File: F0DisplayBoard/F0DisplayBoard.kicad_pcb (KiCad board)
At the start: 2 copper layers, 8 parts, among them J1 NHD-C0216CZ-FSW-FBW-3V3, U1 STM32F051R8T6TR, U2 ROTARY_ENC_PEC12R, U3 AZ1117EH-3.3TRG1, U4 FT232RLREEL, X1 ABLS7M2_16MHz_XTAL

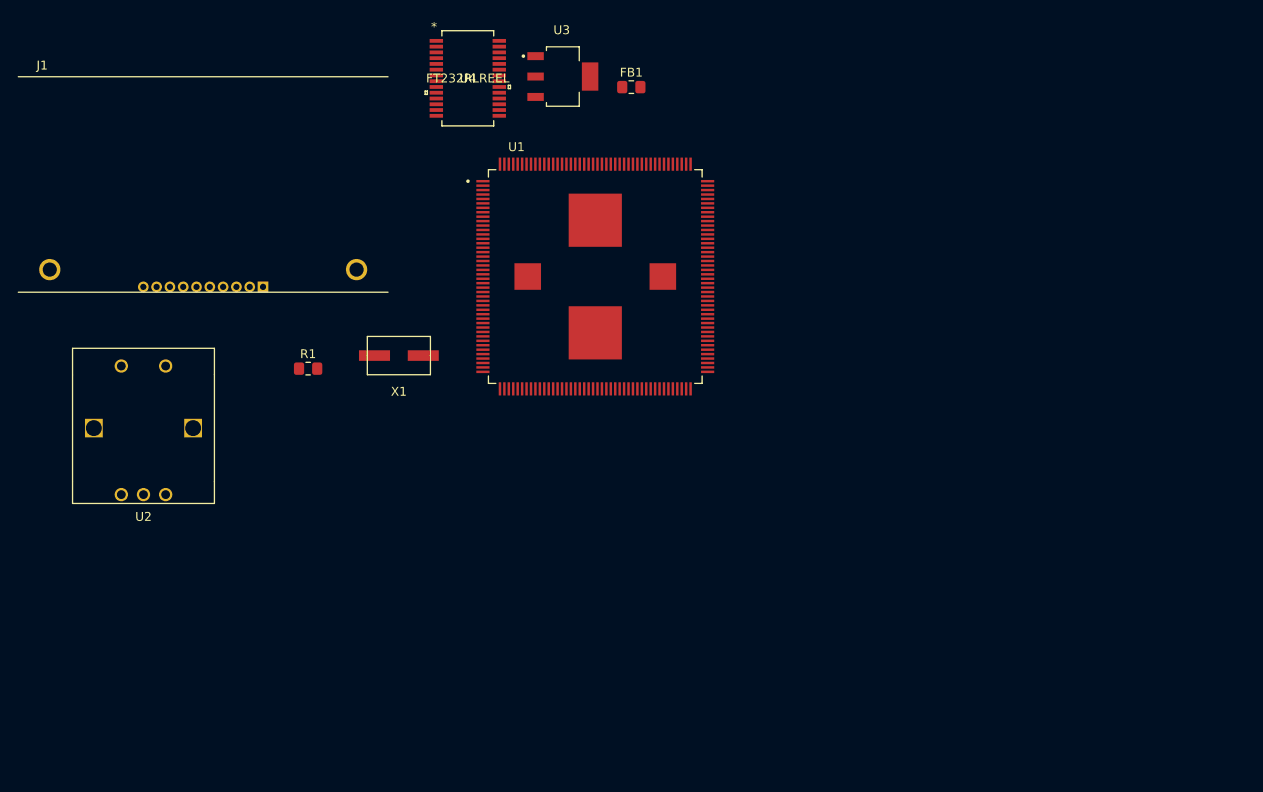
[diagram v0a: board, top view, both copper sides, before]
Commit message: sch: Removed some connectors to make room on board. pcb: rough routing, difficulty with traces cutting into planes. May restart routing of most signals
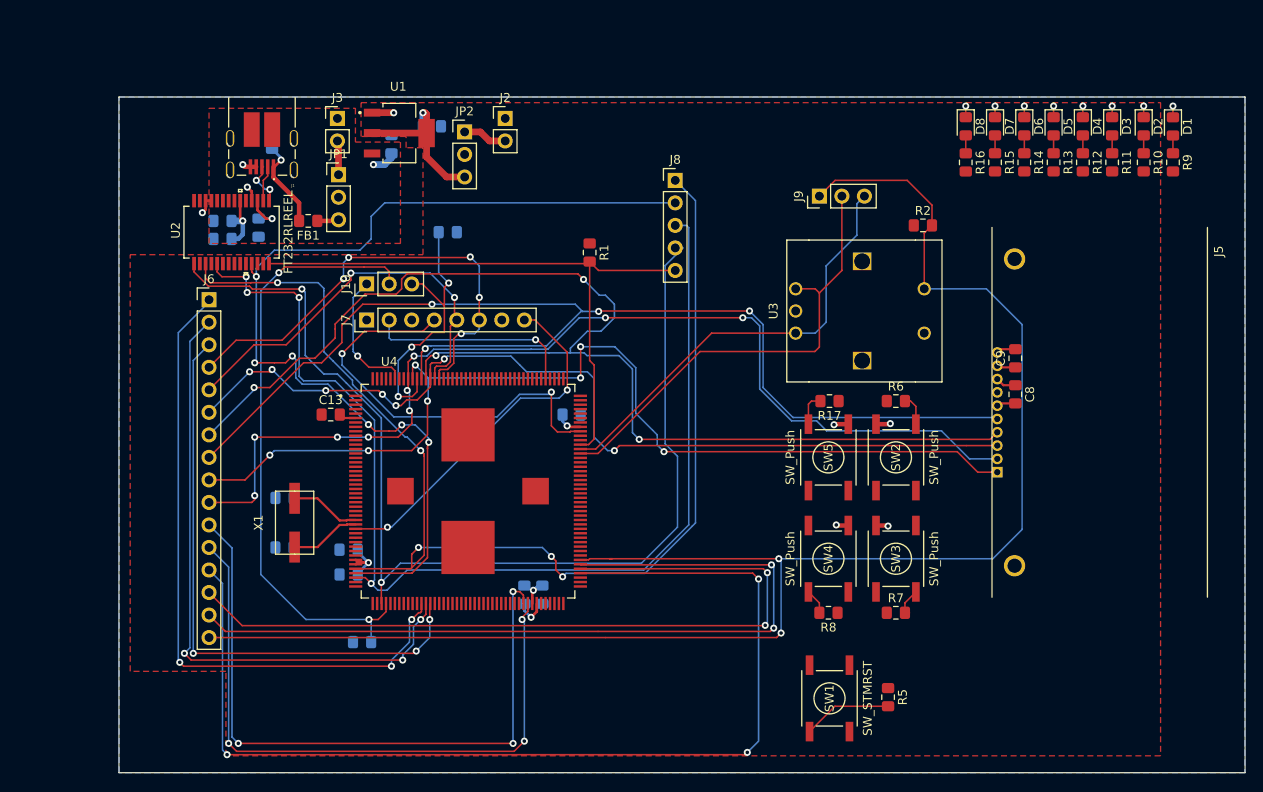
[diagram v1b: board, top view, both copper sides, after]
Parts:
- added C1: 1uF, Capacitor_SMD:C_0805_2012Metric_Pad1.15x1.40mm_HandSolder, B.Cu at (123.4, 70.1)
- added C10: 31pF, Capacitor_SMD:C_0805_2012Metric_Pad1.15x1.40mm_HandSolder, B.Cu at (111.4, 115.6)
- added C11: 100nF, Capacitor_SMD:C_0805_2012Metric_Pad1.15x1.40mm_HandSolder, B.Cu at (140.5, 120.9)
- added C12: 100nF, Capacitor_SMD:C_0805_2012Metric_Pad1.15x1.40mm_HandSolder, B.Cu at (143.8, 100.6)
- added C13: 100nF, Capacitor_SMD:C_0805_2012Metric_Pad1.15x1.40mm_HandSolder, F.Cu at (116.6, 100.6)
- added C14: 4.7uF, Capacitor_SMD:C_0805_2012Metric_Pad1.15x1.40mm_HandSolder, B.Cu at (138.4, 120.9)
- added C15: 10nF, Capacitor_SMD:C_0805_2012Metric_Pad1.15x1.40mm_HandSolder, B.Cu at (118.6, 118.6)
- added C16: 1uF, Capacitor_SMD:C_0805_2012Metric_Pad1.15x1.40mm_HandSolder, B.Cu at (118.6, 115.8)
- added C2: 100nF, Capacitor_SMD:C_0805_2012Metric_Pad1.15x1.40mm_HandSolder, B.Cu at (104.4, 80.8)
- added C3: 10nF, Capacitor_SMD:C_0805_2012Metric_Pad1.15x1.40mm_HandSolder, B.Cu at (110.0, 69.6)
- added C4: 4.7uF, Capacitor_SMD:C_0805_2012Metric_Pad1.15x1.40mm_HandSolder, B.Cu at (104.4, 78.7)
- added C5: 100nF, Capacitor_SMD:C_0805_2012Metric_Pad1.15x1.40mm_HandSolder, B.Cu at (108.5, 79.5)
- added C6: 1uF, Capacitor_SMD:C_0805_2012Metric_Pad1.15x1.40mm_HandSolder, B.Cu at (128.0, 68.1)
- added C7: 31pf, Capacitor_SMD:C_0805_2012Metric_Pad1.15x1.40mm_HandSolder, B.Cu at (111.4, 110.0)
- added C8: 1uF, Capacitor_SMD:C_0805_2012Metric_Pad1.15x1.40mm_HandSolder, F.Cu at (193.8, 98.3)
- added C9: 1uF, Capacitor_SMD:C_0805_2012Metric_Pad1.15x1.40mm_HandSolder, F.Cu at (193.8, 94.2)
- added D1: LED, LED_SMD:LED_0805_2012Metric_Pad1.15x1.40mm_HandSolder, F.Cu at (211.6, 68.1)
- added D2: LED, LED_SMD:LED_0805_2012Metric_Pad1.15x1.40mm_HandSolder, F.Cu at (208.3, 68.1)
- added D3: LED, LED_SMD:LED_0805_2012Metric_Pad1.15x1.40mm_HandSolder, F.Cu at (204.7, 68.1)
- added D4: LED, LED_SMD:LED_0805_2012Metric_Pad1.15x1.40mm_HandSolder, F.Cu at (201.4, 68.1)
- added D5: LED, LED_SMD:LED_0805_2012Metric_Pad1.15x1.40mm_HandSolder, F.Cu at (198.1, 68.1)
- added D6: LED, LED_SMD:LED_0805_2012Metric_Pad1.15x1.40mm_HandSolder, F.Cu at (194.8, 68.1)
- added D7: LED, LED_SMD:LED_0805_2012Metric_Pad1.15x1.40mm_HandSolder, F.Cu at (191.5, 68.1)
- added D8: LED, LED_SMD:LED_0805_2012Metric_Pad1.15x1.40mm_HandSolder, F.Cu at (188.2, 68.1)
- added J1: USB_B_Micro, MICROUSB:CUIDEVICES_UJ2-MIBH-4-SMT-TR, F.Cu at (108.8, 67.7)
- added J10: CONN_STMPWR, Connector_PinHeader_2.54mm:PinHeader_1x03_P2.54mm_Vertical, F.Cu at (120.7, 85.9)
- added J2: CONN_3V3, Connector_PinHeader_2.54mm:PinHeader_1x02_P2.54mm_Vertical, F.Cu at (136.3, 67.2)
- added J3: CONN_5v, Connector_PinHeader_2.54mm:PinHeader_1x02_P2.54mm_Vertical, F.Cu at (117.3, 67.2)
- added J6: CONN_PB, Connector_PinHeader_2.54mm:PinHeader_1x16_P2.54mm_Vertical, F.Cu at (102.9, 87.6)
- added J7: CONN_DEBUG, Connector_PinHeader_2.54mm:PinHeader_1x08_P2.54mm_Vertical, F.Cu at (120.7, 89.9)
- added J8: CONN_FTDI, Connector_PinHeader_2.54mm:PinHeader_1x05_P2.54mm_Vertical, F.Cu at (155.4, 74.2)
- added J9: CONN_ROT, Connector_PinHeader_2.54mm:PinHeader_1x03_P2.54mm_Vertical, F.Cu at (171.7, 75.9)
- added JP1: Jumper_3_Open, Connector_PinHeader_2.54mm:PinHeader_1x03_P2.54mm_Vertical, F.Cu at (117.5, 73.5)
- added JP2: Jumper_3_Open, Connector_PinHeader_2.54mm:PinHeader_1x03_P2.54mm_Vertical, F.Cu at (131.7, 68.7)
- added R1: 1K, Resistor_SMD:R_0805_2012Metric_Pad1.15x1.40mm_HandSolder, F.Cu at (145.8, 82.3)
- added R10: 1K, Resistor_SMD:R_0805_2012Metric_Pad1.15x1.40mm_HandSolder, F.Cu at (208.3, 72.1)
- added R11: 1K, Resistor_SMD:R_0805_2012Metric_Pad1.15x1.40mm_HandSolder, F.Cu at (204.7, 72.1)
- added R12: 1K, Resistor_SMD:R_0805_2012Metric_Pad1.15x1.40mm_HandSolder, F.Cu at (201.4, 72.1)
- added R13: 1K, Resistor_SMD:R_0805_2012Metric_Pad1.15x1.40mm_HandSolder, F.Cu at (198.1, 72.1)
- added R14: 1K, Resistor_SMD:R_0805_2012Metric_Pad1.15x1.40mm_HandSolder, F.Cu at (194.8, 72.1)
- added R15: 1K, Resistor_SMD:R_0805_2012Metric_Pad1.15x1.40mm_HandSolder, F.Cu at (191.5, 72.1)
- added R16: 1K, Resistor_SMD:R_0805_2012Metric_Pad1.15x1.40mm_HandSolder, F.Cu at (188.2, 72.1)
- added R17: 1K, Resistor_SMD:R_0805_2012Metric_Pad1.15x1.40mm_HandSolder, F.Cu at (172.8, 99.1)
- added R3: 10K, Resistor_SMD:R_0805_2012Metric_Pad1.15x1.40mm_HandSolder, B.Cu at (120.1, 126.2)
- added R4: 10K, Resistor_SMD:R_0805_2012Metric_Pad1.15x1.40mm_HandSolder, B.Cu at (129.8, 80.0)
- added R5: 1K, Resistor_SMD:R_0805_2012Metric_Pad1.15x1.40mm_HandSolder, F.Cu at (179.5, 132.5)
- added R6: 1K, Resistor_SMD:R_0805_2012Metric_Pad1.15x1.40mm_HandSolder, F.Cu at (180.3, 99.1)
- added R7: 1K, Resistor_SMD:R_0805_2012Metric_Pad1.15x1.40mm_HandSolder, F.Cu at (180.3, 122.9)
- added R8: 1K, Resistor_SMD:R_0805_2012Metric_Pad1.15x1.40mm_HandSolder, F.Cu at (172.7, 122.9)
- added R9: 1K, Resistor_SMD:R_0805_2012Metric_Pad1.15x1.40mm_HandSolder, F.Cu at (211.6, 72.1)
- added SW1: SW_STMRST, TACTILE_SW:PTS645SK43SMTR92LFS, F.Cu at (172.8, 132.6)
- added SW2: SW_Push, TACTILE_SW:PTS645SK43SMTR92LFS, F.Cu at (180.3, 105.4)
- added SW3: SW_Push, TACTILE_SW:PTS645SK43SMTR92LFS, F.Cu at (180.3, 116.8)
- added SW4: SW_Push, TACTILE_SW:PTS645SK43SMTR92LFS, F.Cu at (172.7, 116.8)
- added SW5: SW_Push, TACTILE_SW:PTS645SK43SMTR92LFS, F.Cu at (172.7, 105.4)
- U1: value STM32F051R8T6TR -> AZ1117EH-3.3TRG1; footprint STM32F051R8T6:QFP50P2600X2600X160-176N -> 3V3_Regulator:SOT230P700X180-4N
- U2: value ROTARY_ENC_PEC12R -> FT232RLREEL; footprint ROTARY_ENC_PEC12R:ROTARY_ENC_PEC12R -> ft232r:FT232RLREEL
- U3: value AZ1117EH-3.3TRG1 -> ROTARY_ENC_PEC12R; footprint 3V3_Regulator:SOT230P700X180-4N -> ROTARY_ENC_PEC12R:ROTARY_ENC_PEC12R
- U4: value FT232RLREEL -> STM32F051R8T6TR; footprint ft232r:FT232RLREEL -> STM32F051R8T6:QFP50P2600X2600X160-176N
- moved J5 90.7 mm to (191.8, 100.3), turned to 270 degrees
- moved R2 71.2 mm to (183.4, 79.2)
- moved U4 46.6 mm to (132.1, 109.2)
- moved U3 42.9 mm to (176.5, 88.9), turned to 270 degrees
- moved FB1 39.4 mm to (114.1, 78.7), turned to 180 degrees
- moved U1 27.4 mm to (124.3, 68.8)
- moved U2 24.2 mm to (105.4, 80.0), turned to 90 degrees
- moved X1 22.2 mm to (112.5, 112.8), turned to 270 degrees
- renumbered J1 to J5, R1 to R2
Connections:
- net Net-(U4-Pad10) renamed /PC15
- net Net-(U4-Pad8) renamed /PC13
- net Net-(U4-Pad9) renamed /PC14
- FB1 pad 1: +5V -> /VUSB
- FB1 pad 2: Net-(C5-Pad1) -> /VBUS
- U1 pad 1: Net-(U1-Pad1) -> GND
- U1 pad 2: Net-(U1-Pad2) -> /3.3V_AZ
- U1 pad 3: Net-(U1-Pad3) -> +5V
- U1 pad 4: Net-(U1-Pad4) -> /3.3V_AZ
- U2 pad 1: /ROT_SW1 -> /FT_TX
- U2 pad 2: GND -> Net-(U2-Pad2)
- U2 pad 3: /ROT_CHA -> /FT_RTS
- U2 pad 4: GND -> +3V3
- U2 pad 5: /ROT_CHB -> /FT_RX
- U3 pad 1: GND -> /ROT_SW1
- U3 pad 2: +3V3 -> GND
- U3 pad 3: +5V -> /ROT_CHA
- U3 pad 4: +3V3 -> GND
- U4 pad 1: /FT_TX -> Net-(U4-Pad1)
- U4 pad 11: /FT_CTS -> Net-(U4-Pad11)
- U4 pad 14: /FT_PWREN -> GND
- U4 pad 15: Net-(J2-Pad3) -> +3V3
- U4 pad 18: GND -> Net-(U4-Pad18)
- U4 pad 20: +5V -> Net-(U4-Pad20)
- U4 pad 21: GND -> Net-(U4-Pad21)
- U4 pad 22: Net-(U4-Pad22) -> GND
- U4 pad 23: Net-(U4-Pad23) -> +3V3
- U4 pad 25: GND -> Net-(U4-Pad25)
- U4 pad 26: GND -> Net-(U4-Pad26)
- U4 pad 3: /FT_RTS -> Net-(U4-Pad3)
- U4 pad 4: +3V3 -> Net-(U4-Pad4)
- U4 pad 5: /FT_RX -> Net-(U4-Pad5)
- U4 pad 6: Net-(U4-Pad6) -> /VBAT
- U4 pad 7: GND -> Net-(U4-Pad7)
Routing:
- net /ROT_SW1: track 0.00 -> 184.9 mm, vias 0 -> 2
- net /DISP_SCL: track 0.00 -> 140.2 mm, vias 0 -> 4
- net /FT_RTS: track 0.00 -> 136.9 mm, vias 0 -> 5
- net /DISP_SI: track 0.00 -> 129.9 mm, vias 0 -> 4
- net /FT_RX: track 0.00 -> 126.7 mm, vias 0 -> 4
- net /FT_TX: track 0.00 -> 124.1 mm, vias 0 -> 2
- net /PB12: track 0.00 -> 120.9 mm, vias 0 -> 3
- net /DISP_RS: track 0.00 -> 117.2 mm, vias 0 -> 9
- net /DISP_RST: track 0.00 -> 114.2 mm, vias 0 -> 7
- net /FT_CTS: track 0.00 -> 112.2 mm, vias 0 -> 6
- net /DISP_CSB: track 0.00 -> 106.3 mm, vias 0 -> 7
- net /PB14: track 0.00 -> 93.4 mm, vias 0 -> 2
- net /PB13: track 0.00 -> 91.6 mm, vias 0 -> 2
- net /PB10: track 0.00 -> 76.4 mm, vias 0 -> 3
- net /PB0: track 0.00 -> 75.0 mm, vias 0 -> 3
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- added copper zone on F.Cu, net +3V3
- added copper zone on F.Cu, net +5V
- added copper zone on B.Cu, net GND
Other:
- board outline added: 127 x 76.2 mm
- rule trace_min: 0.2 -> 0.1778

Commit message: pcb: re-routed mostlyl orthogonally. Still need to get 3.3V plane to reach some pins and check other "unrouted" signals
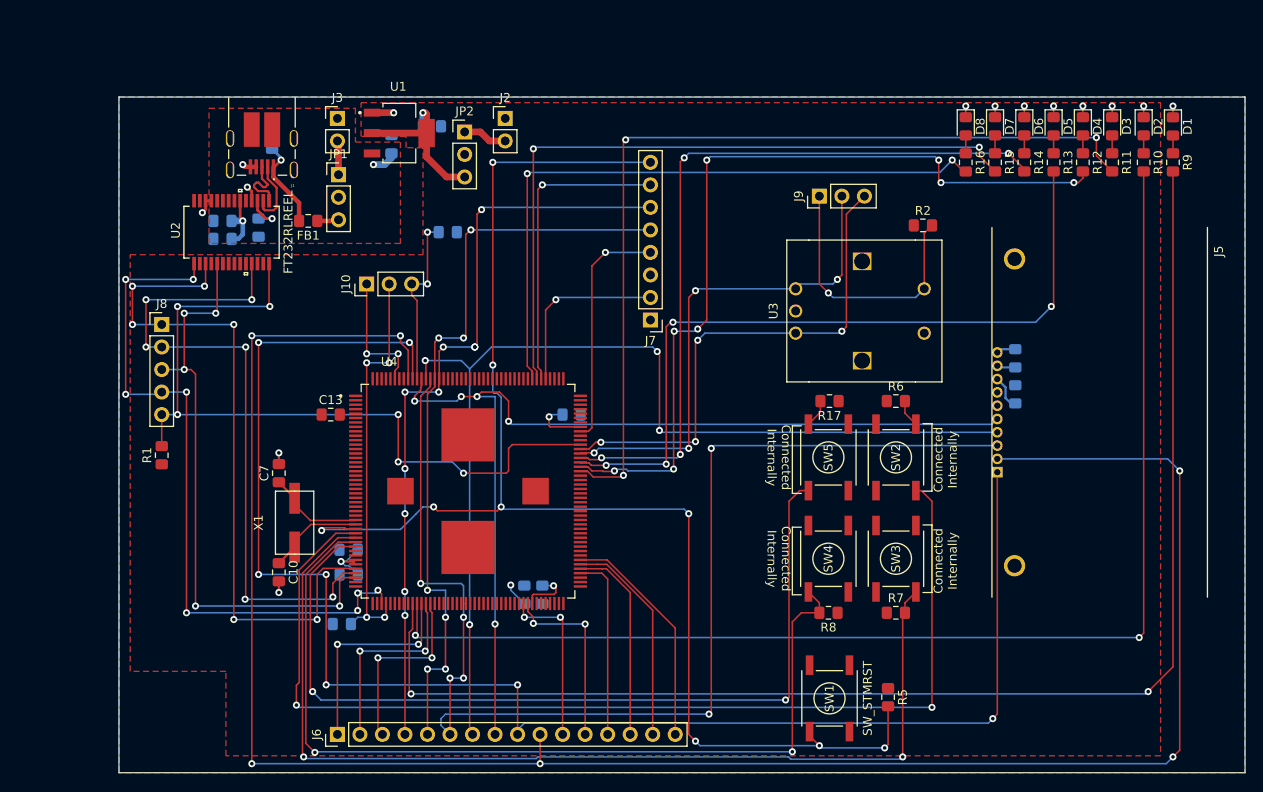
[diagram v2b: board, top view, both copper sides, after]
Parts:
- C10, C7: moved to F.Cu
- C8, C9: moved to B.Cu
- moved J8 60.2 mm to (97.5, 90.4)
- moved R1 53.4 mm to (97.5, 105.2), turned to 90 degrees
- moved J6 51.1 mm to (117.3, 136.7), turned to 90 degrees
- moved J7 32.0 mm to (152.7, 89.9), turned to 180 degrees
- moved R3 3.06 mm to (117.8, 124.2)
- moved C7 2.87 mm to (110.7, 107.2), turned to 90 degrees
- moved C10 2.87 mm to (110.7, 118.4), turned to 270 degrees
- turned C8 to 90 degrees
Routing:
- net /PC4: track 0.00 -> 153.5 mm, vias 0 -> 2
- net /PC5: track 0.00 -> 138.2 mm, vias 0 -> 2
- net /ROT_SW1: track 184.9 -> 56.2 mm, vias 2 -> 1
- net /PC0: track 3.49 -> 123.9 mm, vias 0 -> 2
- net /DISP_RS: track 117.2 -> 231.5 mm, vias 9 -> 6
- net /PC1: track 3.45 -> 115.6 mm, vias 0 -> 2
- net /NRST: track 51.0 -> 159.0 mm, vias 2 -> 9
- net /PC6: track 0.00 -> 100.9 mm, vias 0 -> 3
- net /PB12: track 120.9 -> 20.9 mm, vias 3 -> 0
- net /PC2: track 2.86 -> 102.5 mm, vias 0 -> 2
- net /PC3: track 3.75 -> 101.9 mm, vias 0 -> 2
- net /PC7: track 0.06 -> 95.2 mm, vias 0 -> 8
- net /PC8: track 0.00 -> 85.1 mm, vias 0 -> 4
- net /PC9: track 0.00 -> 84.8 mm, vias 0 -> 4
- net /PC10: track 0.00 -> 79.9 mm, vias 0 -> 2
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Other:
- board text added: "Connected Internally"

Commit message: Rev2 completed   -Added current-limiting resitstor for LCD backlight   -Fixed microcontroller footprint   -Board size reduced
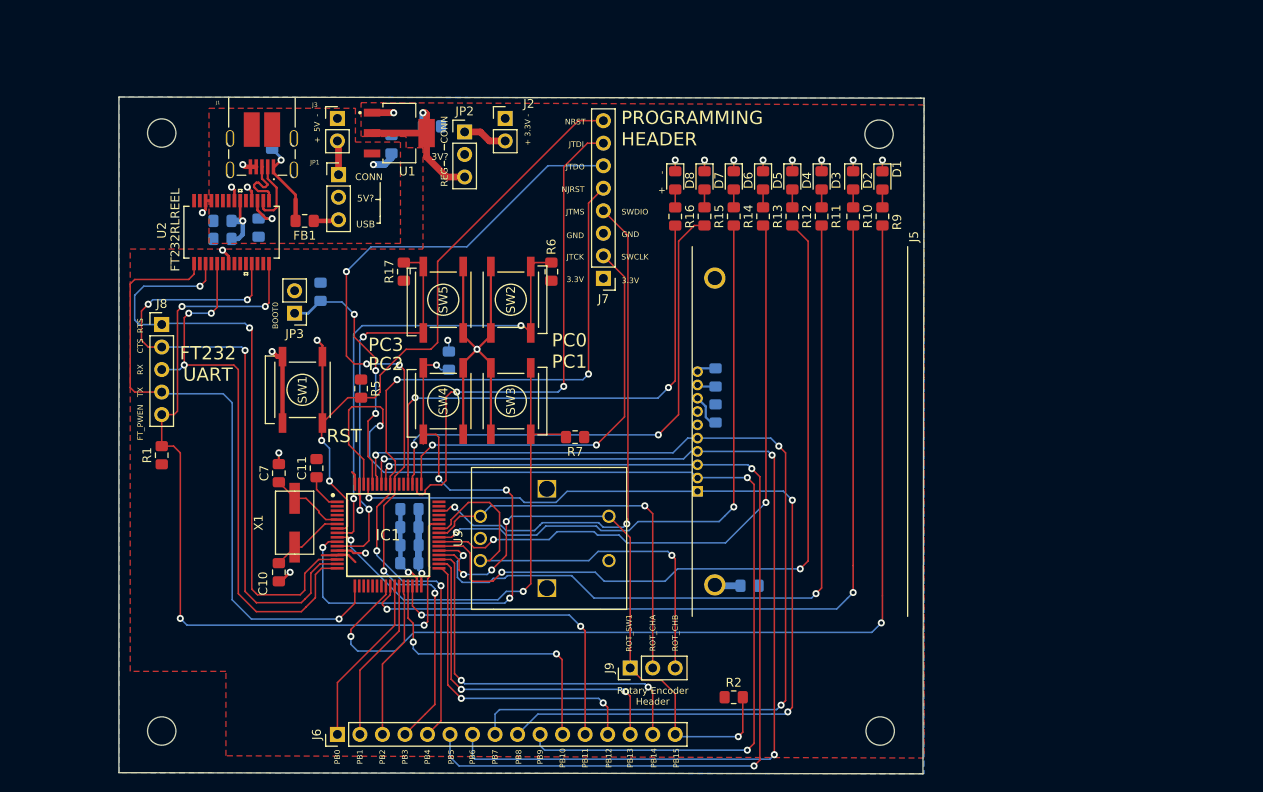
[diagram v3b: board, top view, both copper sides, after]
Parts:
- removed C16: 1uF, Capacitor_SMD:C_0805_2012Metric_Pad1.15x1.40mm_HandSolder
- removed J10: CONN_STMPWR, Connector_PinHeader_2.54mm:PinHeader_1x03_P2.54mm_Vertical
- removed U4: STM32F051R8T6TR, STM32F051R8T6:QFP50P2600X2600X160-176N
- added G***: LOGO, Sophie:sophie, B.Cu at (103.3, 118.1)
- added IC1: STM32F051R8T6TR, LibraryLoader:QFP50P1200X1200X160-64N, F.Cu at (123.1, 114.2)
- added JP3: JUMPER_BOOT0, Connector_PinHeader_2.54mm:PinHeader_1x02_P2.54mm_Vertical, F.Cu at (112.5, 89.2)
- added REF**: MountingHole_3.2mm_M3, MountingHole:MountingHole_3.2mm_M3, F.Cu at (97.5, 68.8)
- added REF**: MountingHole_3.2mm_M3, MountingHole:MountingHole_3.2mm_M3, F.Cu at (178.4, 69.0)
- added REF**: MountingHole_3.2mm_M3, MountingHole:MountingHole_3.2mm_M3, F.Cu at (97.5, 136.3)
- added REF**: MountingHole_3.2mm_M3, MountingHole:MountingHole_3.2mm_M3, F.Cu at (178.6, 136.3)
- C11: moved to F.Cu
- C13: value 100nF -> 4.7uF; moved to B.Cu
- C14: value 4.7uF -> 10nF
- C15: value 10nF -> 1uF
- R3: value 10K -> 1K
- R8: moved to B.Cu
- moved R5 68.9 mm to (120.0, 97.7)
- moved SW1 68.9 mm to (113.4, 97.8), turned to 90 degrees
- moved J9 57.3 mm to (150.4, 129.2)
- moved R2 57.3 mm to (162.0, 132.5)
- moved R8 51.4 mm to (129.9, 94.5), turned to 270 degrees
- moved R17 50.2 mm to (124.8, 84.5), turned to 90 degrees
- moved SW2 46.9 mm to (136.9, 87.6)
- moved SW3 46.9 mm to (136.9, 99.1)
- moved SW4 46.9 mm to (129.3, 99.1)
- moved SW5 46.9 mm to (129.3, 87.6)
- moved R3 46.2 mm to (163.8, 119.9), turned to 0 degrees
- moved U3 43.8 mm to (141.0, 114.6)
- moved R6 41.5 mm to (141.5, 84.5), turned to 90 degrees
- moved R7 41.2 mm to (144.2, 103.1), turned to 180 degrees
- moved C8 33.9 mm to (160.0, 100.5)
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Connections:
- C11 pad 1: /VCAP1 -> /VBAT
- C11 pad 2: GND -> +3V3
- C12 pad 1: GND -> +3V3
- C12 pad 2: /VCAP2 -> GND
- C13 pad 2: /VBAT -> GND
- C15 pad 1: +3.3VA -> +3V3
- J5 pad K: GND -> /DISP_LED-
- R3 pad 1: /BYPASS_REG -> /DISP_LED-
- R4 pad 1: GND -> /BOOT0
- R4 pad 2: /BOOT0 -> GND
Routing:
- net /DISP_RS: track 231.5 -> 119.4 mm, vias 6 -> 3
- net /NRST: track 159.0 -> 76.0 mm, vias 9 -> 3
- net /DISP_RST: track 177.3 -> 106.1 mm, vias 7 -> 3
- net GND: track 20.6 -> 90.4 mm, vias 14 -> 21
- net /PC0: track 123.9 -> 54.9 mm
- net /PC1: track 115.6 -> 54.4 mm
- net /PC3: track 101.9 -> 44.3 mm
- net /BYPASS_REG: track 45.9 -> 0.00 mm, vias 4 -> 0
- net /PC5: track 138.2 -> 98.0 mm
- net /PC4: track 153.5 -> 114.5 mm
- net /PC2: track 102.5 -> 68.9 mm, vias 2 -> 5
- net /JTMS-SWDIO: track 27.0 -> 59.7 mm, vias 1 -> 2
- net /DISP_CSB: track 141.9 -> 114.8 mm, vias 6 -> 3
- net /JTCK-SWCLK: track 20.2 -> 47.1 mm, vias 1 -> 2
- net /JTDI: track 34.4 -> 58.6 mm, vias 1 -> 2
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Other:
- board size 127 x 76.2 mm -> 90.8 x 76.3 mm
- rule trace_min: 0.1778 -> 0
- board text added: "+"
- board text added: "+ 3.3V -"
- board text added: "+ 5V -"
- board text added: "-"
- board text added: "3.3V"
- board text added: "3V?"
- board text added: "5V?"
- board text added: "BOOT0"
- board text added: "CONN"
- board text added: "CTS"
- board text added: "F0 Display Board Rev2 Michael Cupka"
- board text added: "FT232 UART"
- board text added: "FT_PWEN"
- board text added: "GND"
- board text added: "JTCK"
- board text added: "JTDI"
- board text added: "JTDO"
- board text added: "JTMS"
- board text added: "NJRST"
- board text added: "NRST"
- board text added: "PB0"
- board text added: "PB1"
- board text added: "PB10"
- board text added: "PB11"
- board text added: "PB12"
- board text added: "PB13"
- board text added: "PB14"
- board text added: "PB15"
- board text added: "PB2"
- board text added: "PB3"
- board text added: "PB4"
- board text added: "PB5"
- board text added: "PB6"
- board text added: "PB7"
- board text added: "PB8"
- board text added: "PB9"
- board text added: "PC0"
- board text added: "PC1"
- board text added: "PC2"
- board text added: "PC3"
- board text added: "PROGRAMMING HEADER"
- board text added: "REG"
- board text added: "ROT_CHA"
- board text added: "ROT_CHB"
- board text added: "ROT_SW1"
- board text added: "RST"
- board text added: "RTS"
- board text added: "RX"
- board text added: "Rotary Encoder Header"
- board text added: "SWCLK"
- board text added: "SWDIO"
- board text added: "TX"
- board text added: "USB"
- board text removed: "Connected Internally"
